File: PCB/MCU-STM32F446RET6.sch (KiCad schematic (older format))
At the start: 41 parts, among them J3 20021121-00010C4LF, J4 0475890001-MicroUSBPort, P1 CONN_01X20, P2 CONN_01X20, SW1 B3U-1000P, U3 STM32F446RET6_-_TQFP64, X1 ABM3B8.000MHZB2T, X2 ABS07-32.768KHZ-9-T

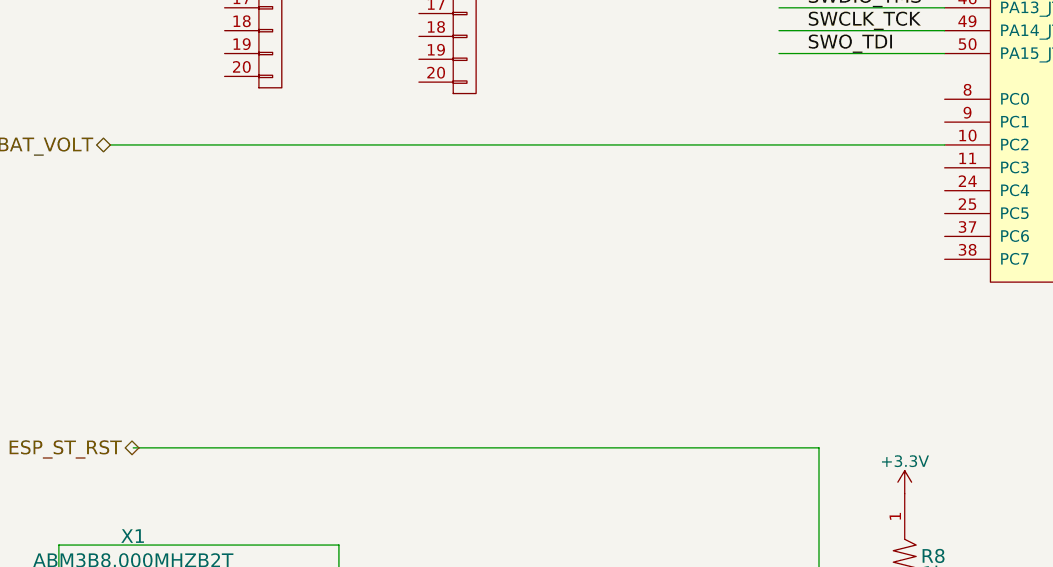
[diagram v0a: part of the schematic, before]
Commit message: Board Layout
Board layout started. ESP8285 component placement preliminary complete.
3D parts added and updated for ESP8285. STM32 and SOT32 3/6 pin
packages.
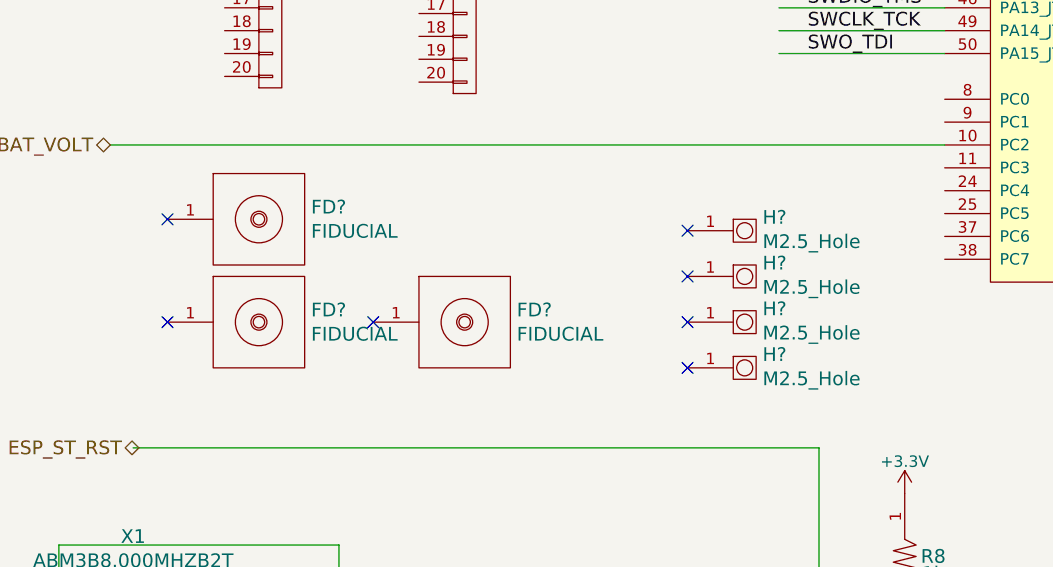
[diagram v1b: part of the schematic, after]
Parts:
- added FD? (x3): FIDUCIAL, PCB_Footprints:FIDUCIAL, symbol FIDUCIAL
- added H? (x4): M2.5_Hole, PCB_Footprints:M2.5_HOLE, symbol M2.5_Hole
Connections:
- no-connect marks 0 -> 7

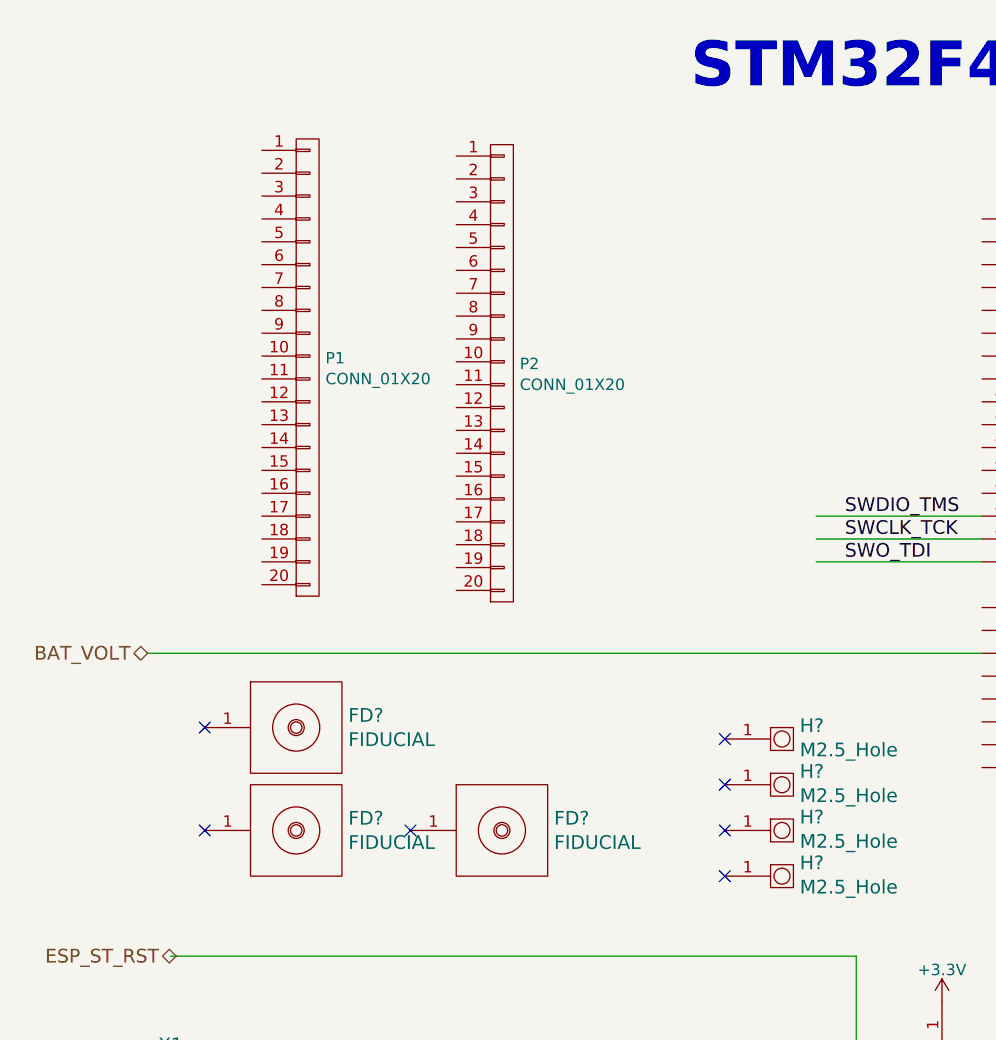
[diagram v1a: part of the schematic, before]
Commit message: Preliminary Formfactor
Preliminary formfactor designed. component placelement still underway
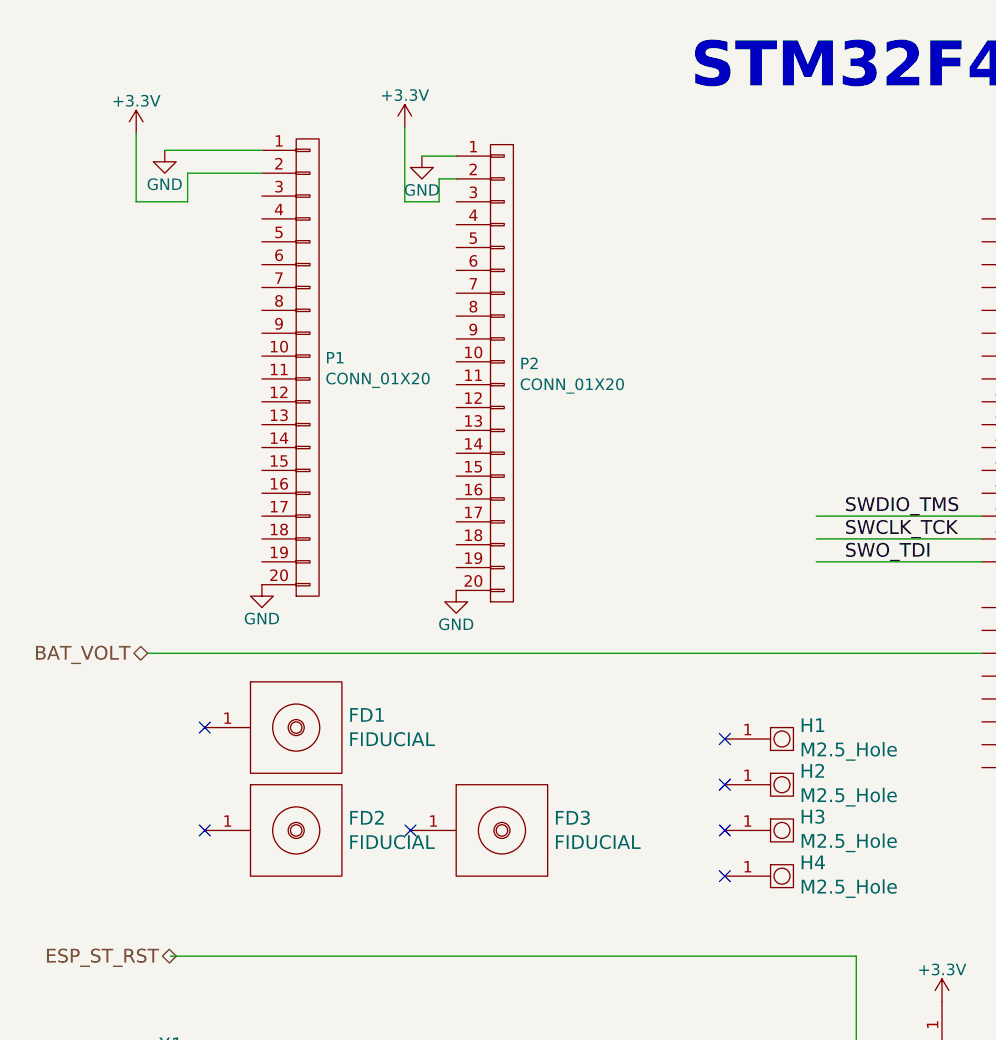
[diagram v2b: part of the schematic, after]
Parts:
- gave numbers to parts that had none: 7
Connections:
- wire segments 103 -> 113
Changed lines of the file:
@@
 $EndComp
 $Comp
-L GND #PWR08
+L GND #PWR11
 U 1 1 57D43B63
 P 1125 6625
-F 0 "#PWR08" H 1125 6375 50  0001 C CNN
+F 0 "#PWR11" H 1125 6375 50  0001 C CNN
 F 1 "GND" H 1125 6475 50  0000 C CNN
 F 2 "" H 1125 6625 50  0000 C CNN
@@
 $EndComp
 $Comp
-L GND #PWR09
+L GND #PWR12
 U 1 1 57D43E04
 P 1450 7325
-F 0 "#PWR09" H 1450 7075 50  0001 C CNN
+F 0 "#PWR12" H 1450 7075 50  0001 C CNN
 F 1 "GND" H 1450 7175 50  0000 C CNN
 F 2 "" H 1450 7325 50  0000 C CNN
@@
 $EndComp
 $Comp
-L +3.3V #PWR010
+L +3.3V #PWR8
 U 1 1 57D443BB
 P 575 6175
-F 0 "#PWR010" H 575 6025 50  0001 C CNN
+F 0 "#PWR8" H 575 6025 50  0001 C CNN
 F 1 "+3.3V" H 575 6315 50  0000 C CNN
 F 2 "" H 575 6175 50  0000 C CNN
@@
 $EndComp
 $Comp
-L +3.3V #PWR011
+L +3.3V #PWR9
 U 1 1 57D444DD
 P 575 6875
-F 0 "#PWR011" H 575 6725 50  0001 C CNN
+F 0 "#PWR9" H 575 6725 50  0001 C CNN
 F 1 "+3.3V" H 575 7015 50  0000 C CNN
 F 2 "" H 575 6875 50  0000 C CNN
@@
 $EndComp
 $Comp
-L GND #PWR012
+L GND #PWR18
 U 1 1 57D449FF
 P 5125 5875
-F 0 "#PWR012" H 5125 5625 50  0001 C CNN
+F 0 "#PWR18" H 5125 5625 50  0001 C CNN
 F 1 "GND" H 5125 5725 50  0000 C CNN
 F 2 "" H 5125 5875 50  0000 C CNN
@@
 $EndComp
 $Comp
-L +3.3V #PWR013
+L +3.3V #PWR17
 U 1 1 57D45F91
 P 4450 4875
-F 0 "#PWR013" H 4450 4725 50  0001 C CNN
+F 0 "#PWR17" H 4450 4725 50  0001 C CNN
 F 1 "+3.3V" H 4450 5015 50  0000 C CNN
 F 2 "" H 4450 4875 50  0000 C CNN
@@
 $EndComp
 $Comp
-L GND #PWR014
+L GND #PWR15
 U 1 1 57D46AC6
 P 3825 7325
-F 0 "#PWR014" H 3825 7075 50  0001 C CNN
+F 0 "#PWR15" H 3825 7075 50  0001 C CNN
 F 1 "GND" H 3825 7175 50  0000 C CNN
 F 2 "" H 3825 7325 50  0000 C CNN
@@
 $EndComp
 $Comp
-L GND #PWR015
+L GND #PWR16
 U 1 1 57D47BC2
 P 4225 7325
-F 0 "#PWR015" H 4225 7075 50  0001 C CNN
+F 0 "#PWR16" H 4225 7075 50  0001 C CNN
 F 1 "GND" H 4225 7175 50  0000 C CNN
 F 2 "" H 4225 7325 50  0000 C CNN
@@
 $EndComp
 $Comp
-L GND #PWR016
+L GND #PWR10
 U 1 1 57D49635
 P 1075 5700
-F 0 "#PWR016" H 1075 5450 50  0001 C CNN
+F 0 "#PWR10" H 1075 5450 50  0001 C CNN
 F 1 "GND" H 1075 5550 50  0000 C CNN
 F 2 "" H 1075 5700 50  0000 C CNN
@@
 $EndComp
 $Comp
-L GND #PWR017
+L GND #PWR20
 U 1 1 57D4B2EA
 P 6850 4450
-F 0 "#PWR017" H 6850 4200 50  0001 C CNN
+F 0 "#PWR20" H 6850 4200 50  0001 C CNN
 F 1 "GND" H 6850 4300 50  0000 C CNN
 F 2 "" H 6850 4450 50  0000 C CNN
@@
 $EndComp
 $Comp
-L GND #PWR018
+L GND #PWR14
 U 1 1 57D4C07E
 P 1725 6300
-F 0 "#PWR018" H 1725 6050 50  0001 C CNN
+F 0 "#PWR14" H 1725 6050 50  0001 C CNN
 F 1 "GND" H 1725 6150 50  0000 C CNN
 F 2 "" H 1725 6300 50  0000 C CNN
@@
 $EndComp
 $Comp
-L GND #PWR019
+L GND #PWR23
 U 1 1 57D53F54
 P 8325 1150
-F 0 "#PWR019" H 8325 900 50  0001 C CNN
+F 0 "#PWR23" H 8325 900 50  0001 C CNN
 F 1 "GND" H 8325 1000 50  0000 C CNN
 F 2 "" H 8325 1150 50  0000 C CNN
@@
 $EndComp
 $Comp
-L GND #PWR020
+L GND #PWR28
 U 1 1 57D5C6D5
 P 10225 4150
-F 0 "#PWR020" H 10225 3900 50  0001 C CNN
+F 0 "#PWR28" H 10225 3900 50  0001 C CNN
 F 1 "GND" H 10225 4000 50  0000 C CNN
 F 2 "" H 10225 4150 50  0000 C CNN
@@
 $EndComp
 $Comp
-L GND #PWR021
+L GND #PWR26
 U 1 1 57D5C856
 P 9525 4250
-F 0 "#PWR021" H 9525 4000 50  0001 C CNN
+F 0 "#PWR26" H 9525 4000 50  0001 C CNN
 F 1 "GND" H 9525 4100 50  0000 C CNN
 F 2 "" H 9525 4250 50  0000 C CNN
@@
 $EndComp
 $Comp
-L GND #PWR022
+L GND #PWR27
 U 1 1 57D5C8C7
 P 9725 3150
-F 0 "#PWR022" H 9725 2900 50  0001 C CNN
+F 0 "#PWR27" H 9725 2900 50  0001 C CNN
 F 1 "GND" H 9725 3000 50  0000 C CNN
 F 2 "" H 9725 3150 50  0000 C CNN
@@
 $EndComp
 $Comp
-L GND #PWR023
+L GND #PWR25
 U 1 1 57D5FF55
 P 9125 3500
-F 0 "#PWR023" H 9125 3250 50  0001 C CNN
+F 0 "#PWR25" H 9125 3250 50  0001 C CNN
 F 1 "GND" H 9125 3350 50  0000 C CNN
 F 2 "" H 9125 3500 50  0000 C CNN
@@
 $EndComp
 $Comp
-L +3.3V #PWR024
+L +3.3V #PWR22
 U 1 1 57D61D70
 P 8300 5075
-F 0 "#PWR024" H 8300 4925 50  0001 C CNN
+F 0 "#PWR22" H 8300 4925 50  0001 C CNN
 F 1 "+3.3V" H 8300 5215 50  0000 C CNN
 F 2 "" H 8300 5075 50  0000 C CNN
@@
 STM32F446RET6 Main MCU
 $Comp
-L +3.3V #PWR025
+L +3.3V #PWR13
 U 1 1 57D91770
 P 1725 5850
-F 0 "#PWR025" H 1725 5700 50  0001 C CNN
+F 0 "#PWR13" H 1725 5700 50  0001 C CNN
 F 1 "+3.3V" H 1725 5990 50  0000 C CNN
 F 2 "" H 1725 5850 50  0000 C CNN
@@
 $EndComp
 $Comp
-L GND #PWR026
+L GND #PWR21
 U 1 1 57DDB978
 P 8225 6175
-F 0 "#PWR026" H 8225 5925 50  0001 C CNN
+F 0 "#PWR21" H 8225 5925 50  0001 C CNN
 F 1 "GND" H 8225 6025 50  0000 C CNN
 F 2 "" H 8225 6175 50  0000 C CNN
@@
 HEARTBEAT
 $Comp
-L GND #PWR027
+L GND #PWR19
 U 1 1 57E11BCD
 P 5950 5375
-F 0 "#PWR027" H 5950 5125 50  0001 C CNN
+F 0 "#PWR19" H 5950 5125 50  0001 C CNN
 F 1 "GND" H 5950 5225 50  0000 C CNN
 F 2 "" H 5950 5375 50  0000 C CNN
@@
 $EndComp
 $Comp
-L +3.3V #PWR028
+L +3.3V #PWR24
 U 1 1 57E391E0
 P 8900 775
-F 0 "#PWR028" H 8900 625 50  0001 C CNN
+F 0 "#PWR24" H 8900 625 50  0001 C CNN
 F 1 "+3.3V" H 8900 915 50  0000 C CNN
 F 2 "" H 8900 775 50  0000 C CNN
@@
 $EndComp
 $Comp
-L FIDUCIAL FD?
+L FIDUCIAL FD1
 U 1 1 57ED89D0
 P 1425 3675
-F 0 "FD?" H 1853 3728 60  0000 L CNN
+F 0 "FD1" H 1853 3728 60  0000 L CNN
 F 1 "FIDUCIAL" H 1853 3622 60  0000 L CNN
 F 2 "PCB_Footprints:FIDUCIAL" H 1900 4275 197 0001 C CNN
@@
 $EndComp
 $Comp
-L FIDUCIAL FD?
+L FIDUCIAL FD2
 U 1 1 57ED8E83
 P 1425 4125
-F 0 "FD?" H 1853 4178 60  0000 L CNN
+F 0 "FD2" H 1853 4178 60  0000 L CNN
 F 1 "FIDUCIAL" H 1853 4072 60  0000 L CNN
 F 2 "PCB_Footprints:FIDUCIAL" H 1900 4725 197 0001 C CNN
@@
 $EndComp
 $Comp
-L FIDUCIAL FD?
+L FIDUCIAL FD3
 U 1 1 57ED9011
 P 2325 4125
-F 0 "FD?" H 2753 4178 60  0000 L CNN
+F 0 "FD3" H 2753 4178 60  0000 L CNN
 F 1 "FIDUCIAL" H 2753 4072 60  0000 L CNN
 F 2 "PCB_Footprints:FIDUCIAL" H 2800 4725 197 0001 C CNN
@@
 NoConn ~ 1225 3675
 $Comp
-L M2.5_Hole H?
+L M2.5_Hole H1
 U 1 1 57ED9617
 P 3750 3725
-F 0 "H?" H 3828 3783 60  0000 L CNN
+F 0 "H1" H 3828 3783 60  0000 L CNN
 F 1 "M2.5_Hole" H 3828 3677 60  0000 L CNN
 F 2 "PCB_Footprints:M2.5_HOLE" H 3375 4175 197 0001 C CNN
@@
 $EndComp
 $Comp
-L M2.5_Hole H?
+L M2.5_Hole H2
 U 1 1 57ED9C4D
 P 3750 3925
-F 0 "H?" H 3828 3983 60  0000 L CNN
+F 0 "H2" H 3828 3983 60  0000 L CNN
 F 1 "M2.5_Hole" H 3828 3877 60  0000 L CNN
 F 2 "PCB_Footprints:M2.5_HOLE" H 3375 4375 197 0001 C CNN
@@
 $EndComp
 $Comp
-L M2.5_Hole H?
+L M2.5_Hole H3
 U 1 1 57ED9CF6
 P 3750 4125
-F 0 "H?" H 3828 4183 60  0000 L CNN
+F 0 "H3" H 3828 4183 60  0000 L CNN
 F 1 "M2.5_Hole" H 3828 4077 60  0000 L CNN
 F 2 "PCB_Footprints:M2.5_HOLE" H 3375 4575 197 0001 C CNN
@@
 $EndComp
 $Comp
-L M2.5_Hole H?
+L M2.5_Hole H4
 U 1 1 57ED9DA2
 P 3750 4325
-F 0 "H?" H 3828 4383 60  0000 L CNN
+F 0 "H4" H 3828 4383 60  0000 L CNN
 F 1 "M2.5_Hole" H 3828 4277 60  0000 L CNN
 F 2 "PCB_Footprints:M2.5_HOLE" H 3375 4775 197 0001 C CNN
@@
 NoConn ~ 3500 4125
 NoConn ~ 3500 4325
+$Comp
+L GND #PWR?
+U 1 1 57EDF5CF
+P 1475 3050
+F 0 "#PWR?" H 1475 2800 50  0001 C CNN
+F 1 "GND" H 1475 2900 50  0000 C CNN
+F 2 "" H 1475 3050 50  0000 C CNN
+F 3 "" H 1475 3050 50  0000 C CNN
+	1    1475 3050
+	1    0    0    -1
+$EndComp
+$Comp
+L GND #PWR?
+U 1 1 57EDFD82
+P 2325 3075
+F 0 "#PWR?" H 2325 2825 50  0001 C CNN
+F 1 "GND" H 2325 2925 50  0000 C CNN
+F 2 "" H 2325 3075 50  0000 C CNN
+F 3 "" H 2325 3075 50  0000 C CNN
+	1    2325 3075
+	1    0    0    -1
+$EndComp
+$Comp
+L GND #PWR?
+U 1 1 57EDFE20
+P 2175 1175
+F 0 "#PWR?" H 2175 925 50  0001 C CNN
+F 1 "GND" H 2175 1025 50  0000 C CNN
+F 2 "" H 2175 1175 50  0000 C CNN
+F 3 "" H 2175 1175 50  0000 C CNN
+	1    2175 1175
+	1    0    0    -1
+$EndComp
+$Comp
+L GND #PWR?
+U 1 1 57EE05A2
+P 1050 1150
+F 0 "#PWR?" H 1050 900 50  0001 C CNN
+F 1 "GND" H 1050 1000 50  0000 C CNN
+F 2 "" H 1050 1150 50  0000 C CNN
+F 3 "" H 1050 1150 50  0000 C CNN
+	1    1050 1150
+	1    0    0    -1
+$EndComp
+Wire Wire Line
+	2325 1175 2175 1175
+Wire Wire Line
+	1050 1150 1475 1150
+Wire Wire Line
+	1475 1250 1150 1250
+Wire Wire Line
+	1150 1250 1150 1375
+Wire Wire Line
+	1150 1375 925  1375
+Wire Wire Line
+	925  1375 925  1075
+Wire Wire Line
+	2325 1275 2250 1275
+Wire Wire Line
+	2250 1275 2250 1375
+Wire Wire Line
+	2250 1375 2100 1375
+Wire Wire Line
+	2100 1375 2100 1050
+$Comp
+L +3.3V #PWR?
+U 1 1 57EE1246
+P 925 1075
+F 0 "#PWR?" H 925 925 50  0001 C CNN
+F 1 "+3.3V" H 925 1215 50  0000 C CNN
+F 2 "" H 925 1075 50  0000 C CNN
+F 3 "" H 925 1075 50  0000 C CNN
+	1    925  1075
+	1    0    0    -1
+$EndComp
+$Comp
+L +3.3V #PWR?
+U 1 1 57EE1AEF
+P 2100 1050
+F 0 "#PWR?" H 2100 900 50  0001 C CNN
+F 1 "+3.3V" H 2100 1190 50  0000 C CNN
+F 2 "" H 2100 1050 50  0000 C CNN
+F 3 "" H 2100 1050 50  0000 C CNN
+	1    2100 1050
+	1    0    0    -1
+$EndComp
 $EndSCHEMATC

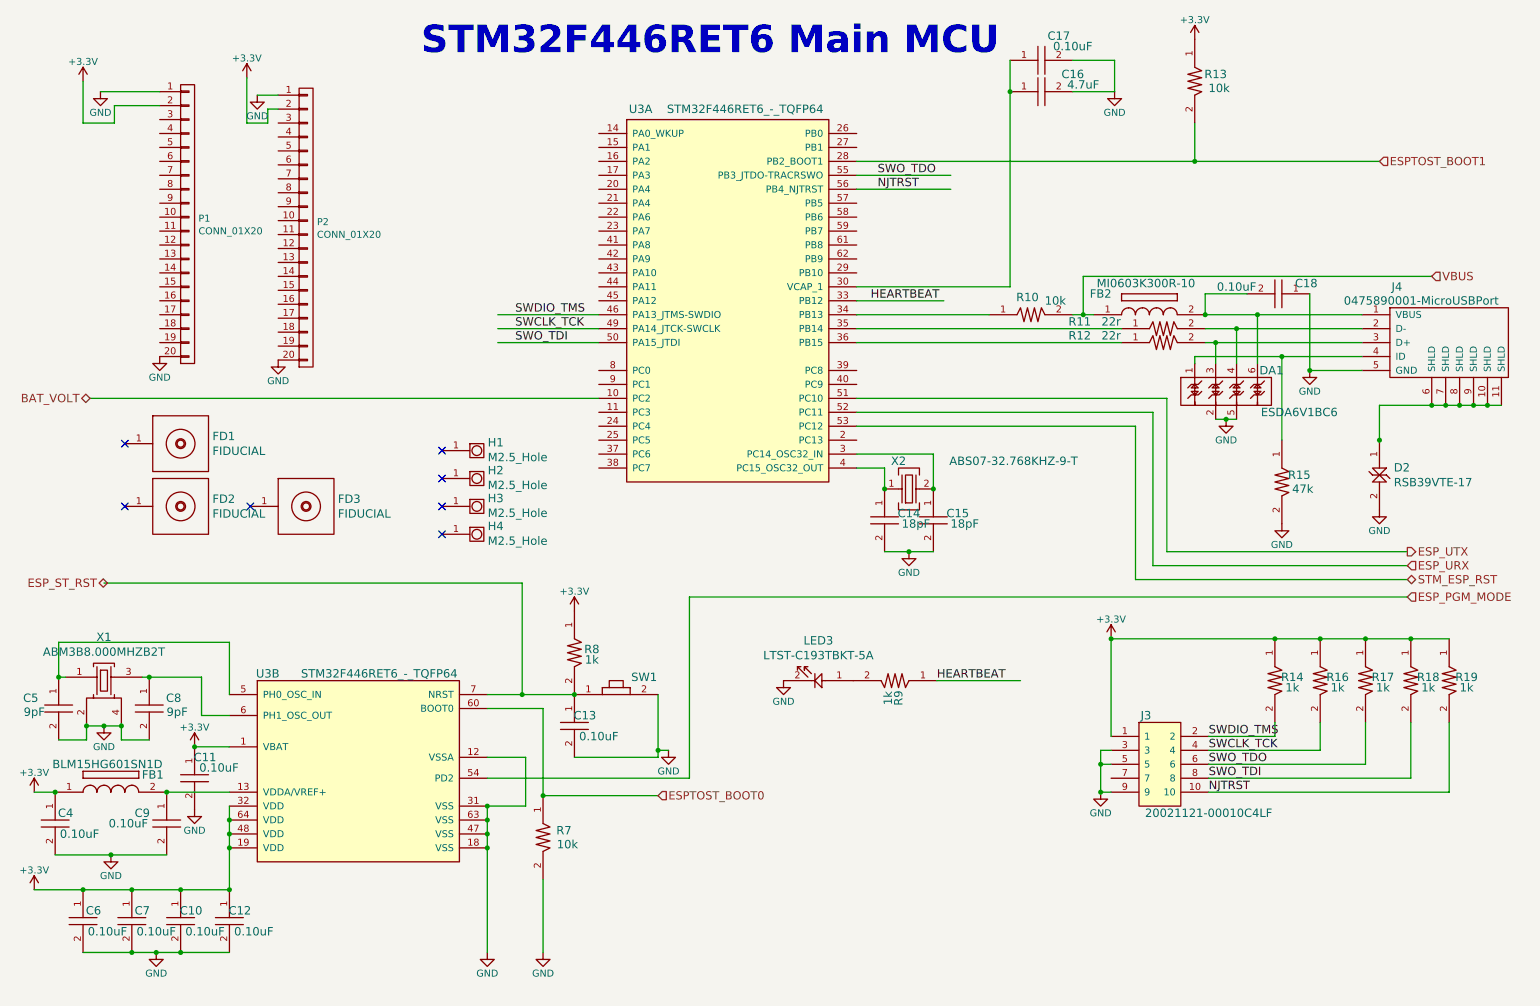
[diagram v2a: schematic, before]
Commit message: Finished Placement and Mapping
Components placed, some routing completed. pin header mapping figured
out.
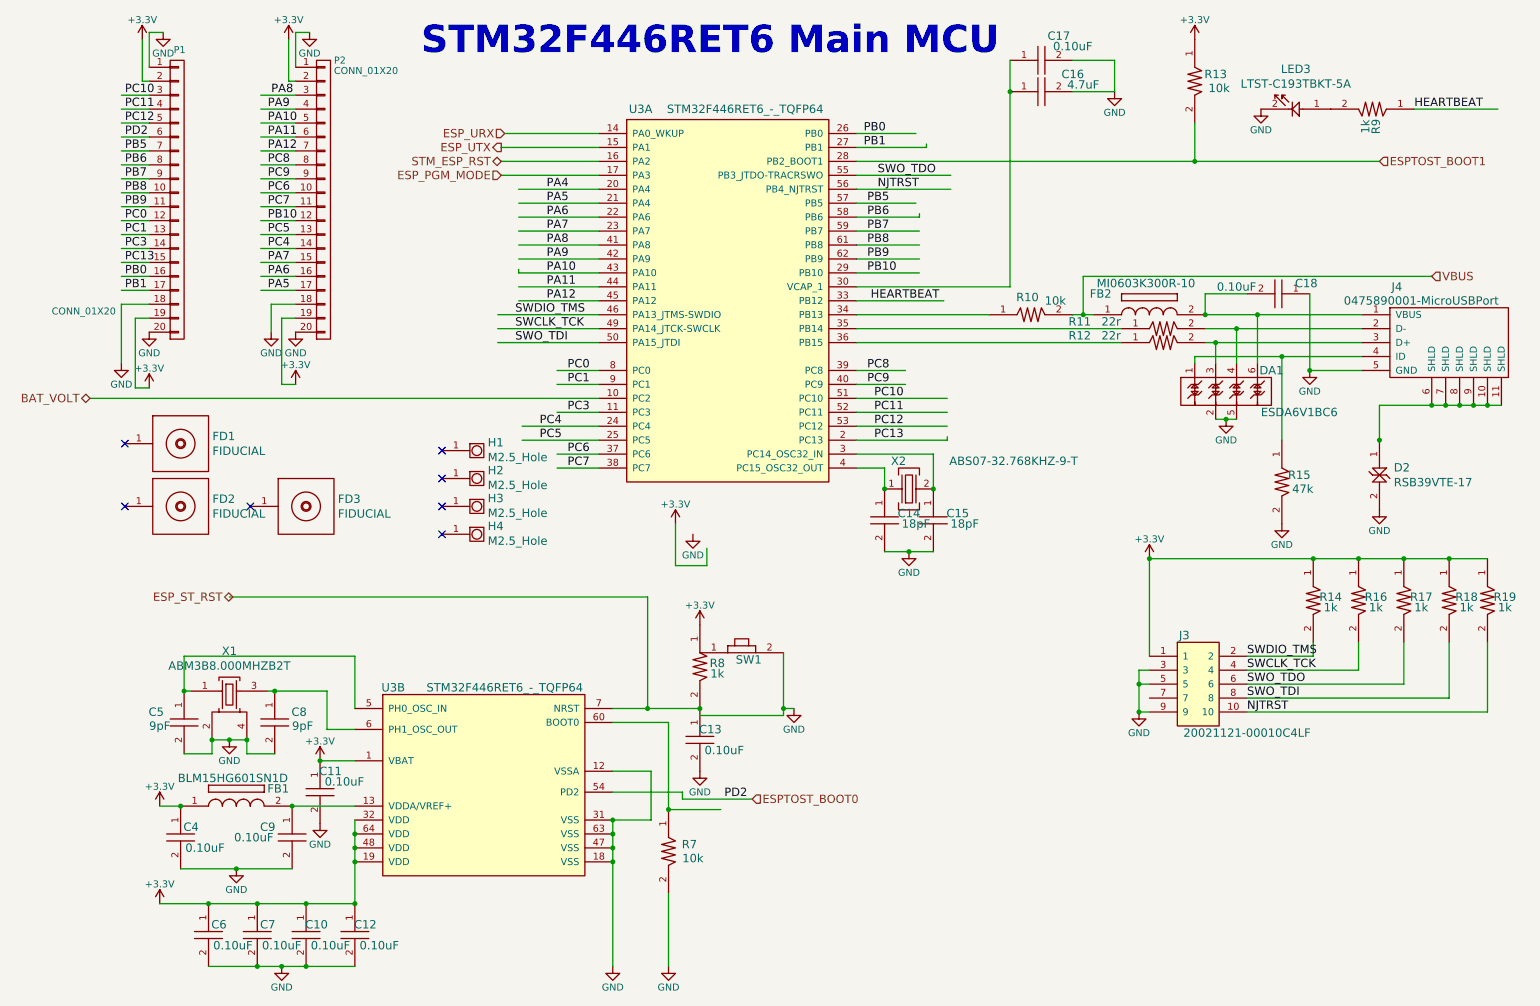
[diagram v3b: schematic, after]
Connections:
- net labels added: PA10, PA11, PA12, PA4, PA5, PA6, PA7, PA8, PA9, PB0, PB1, PB10, PB5, PB6, PB7, PB8, PB9, PC0, PC1, PC10, PC11, PC12, PC13, PC3, PC4, PC5, PC6, PC7, PC8, PC9, PD2
- wire segments 113 -> 183
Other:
- moved on the sheet: C10, C11, C12, C13, C4, C5, C6, C7, C8, C9, FB1, J3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
